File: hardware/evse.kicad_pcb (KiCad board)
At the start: 2 copper layers, 42.5 x 62.5 mm, 85 parts, among them J101 Boot, P101 CON-SENSOR2, P102 Relay, P104 12V/Motor/GP, P105 CP/PP/PE, U101 XMC1100, U102 PEM1-S12-D12-S, U103 MAX14850, U104 ADS1118I, U105 OPA171AIDBV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

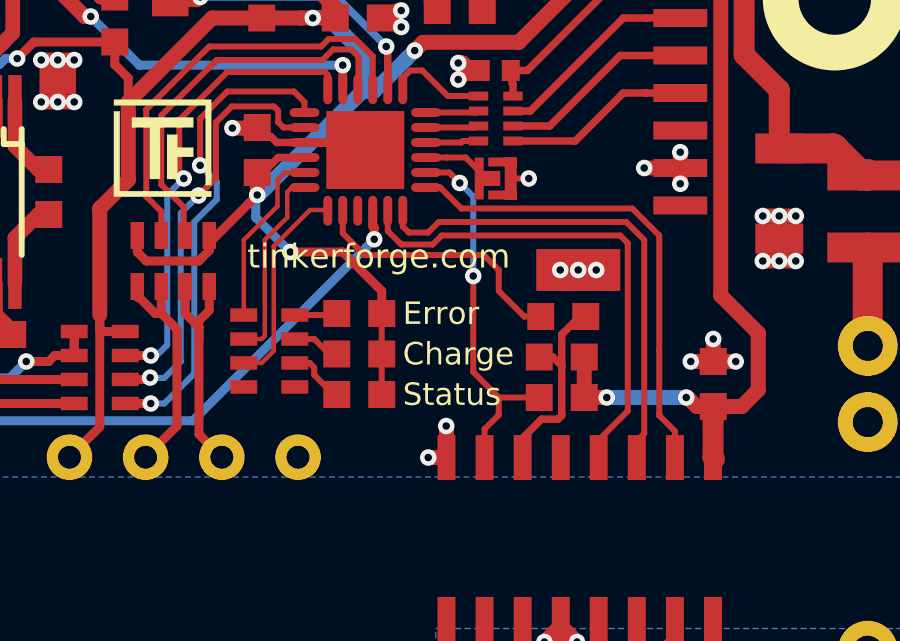
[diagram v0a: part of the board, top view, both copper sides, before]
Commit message: fix m-cs and pwm signal shift
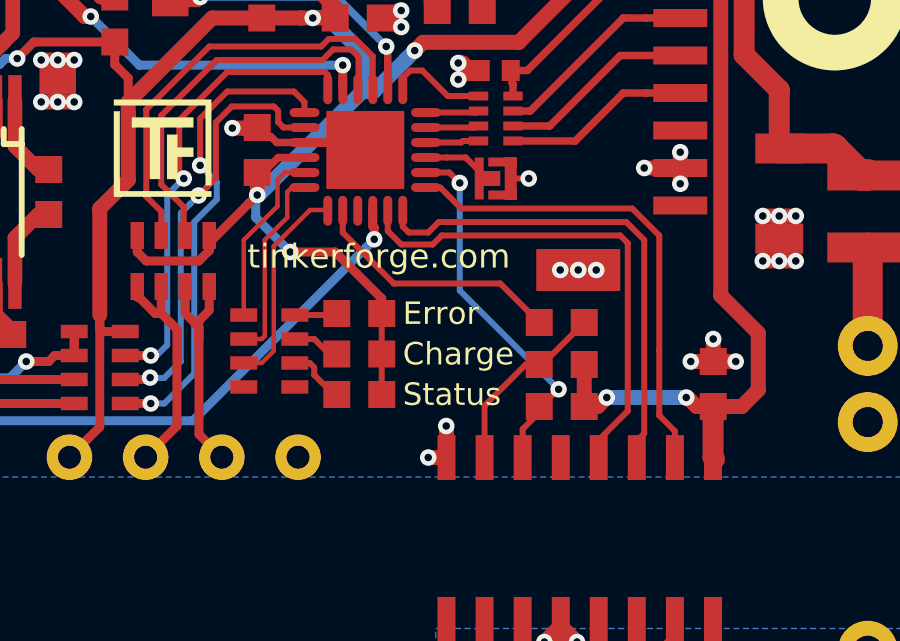
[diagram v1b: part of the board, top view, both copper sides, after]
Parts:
- moved R102 1.65 mm to (168.9, 85.0)
- moved R103 1.10 mm to (168.9, 83.7)
- moved R101 0.21 mm to (168.9, 82.2)
- renumbered Ce to C105
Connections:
- R102 pad 1: Net-(R101-Pad1) -> M-CS
- R103 pad 1: M-CS -> Net-(R101-Pad1)
- U103 pad 6: Net-(R101-Pad1) -> M-CS
- U103 pad 7: M-CS -> Net-(R101-Pad1)
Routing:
- net Net-(R101-Pad1): track 6.83 -> 6.16 mm

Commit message: thermal improvement
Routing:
- net GND: track 85.9 -> 92.1 mm, vias 96 -> 107
- net AGND: track 79.8 -> 81.4 mm, vias 36 -> 39
- added copper zone on F.Cu, net AGND
- added copper zone on F.Cu, net GND
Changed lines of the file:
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@@
     (thickness 1.6)
     (drawings 11)
-    (tracks 1064)
+    (tracks 1094)
     (zones 0)
     (modules 85)
@@
   (layers
     (0 F.Cu signal)
-    (31 B.Cu signal)
+    (31 B.Cu signal hide)
     (32 B.Adhes user)
     (33 F.Adhes user)
@@
   (segment (start 144.1 68.95) (end 144.65 69.5) (width 0.5) (layer F.Cu) (net 2))
   (via (at 144.65 69.5) (size 0.55) (drill 0.25) (layers F.Cu B.Cu) (net 2))
+  (via (at 161.45 69.8) (size 0.55) (drill 0.25) (layers F.Cu B.Cu) (net 2))
+  (segment (start 162 69.8) (end 161.45 69.8) (width 0.5) (layer F.Cu) (net 2))
+  (via (at 160.9 69.8) (size 0.55) (drill 0.25) (layers F.Cu B.Cu) (net 2))
+  (segment (start 161.45 69.8) (end 160.9 69.8) (width 0.5) (layer F.Cu) (net 2))
+  (via (at 160.35 69.8) (size 0.55) (drill 0.25) (layers F.Cu B.Cu) (net 2))
+  (segment (start 160.9 69.8) (end 160.35 69.8) (width 0.5) (layer F.Cu) (net 2))
+  (via (at 162 68.15) (size 0.55) (drill 0.25) (layers F.Cu B.Cu) (net 2))
+  (segment (start 162 68.7) (end 162 68.15) (width 0.5) (layer F.Cu) (net 2))
+  (via (at 161.45 68.15) (size 0.55) (drill 0.25) (layers F.Cu B.Cu) (net 2))
+  (segment (start 162 68.15) (end 161.45 68.15) (width 0.5) (layer F.Cu) (net 2))
+  (via (at 162.55 68.15) (size 0.55) (drill 0.25) (layers F.Cu B.Cu) (net 2))
+  (segment (start 162 68.15) (end 162.55 68.15) (width 0.5) (layer F.Cu) (net 2))
+  (via (at 160.082553 69.309927) (size 0.55) (drill 0.25) (layers F.Cu B.Cu) (net 2))
+  (segment (start 160.35 69.8) (end 160.35 69.577374) (width 0.5) (layer F.Cu) (net 2))
+  (segment (start 160.35 69.577374) (end 160.082553 69.309927) (width 0.5) (layer F.Cu) (net 2))
+  (via (at 160.082553 70.290073) (size 0.55) (drill 0.25) (layers F.Cu B.Cu) (net 2))
+  (segment (start 160.35 69.8) (end 160.35 70.022626) (width 0.5) (layer F.Cu) (net 2))
+  (segment (start 160.35 70.022626) (end 160.082553 70.290073) (width 0.5) (layer F.Cu) (net 2))
+  (via (at 160.9 68.15) (size 0.55) (drill 0.25) (layers F.Cu B.Cu) (net 2))
+  (segment (start 161.45 68.15) (end 160.9 68.15) (width 0.5) (layer F.Cu) (net 2))
+  (via (at 163.1 68.15) (size 0.55) (drill 0.25) (layers F.Cu B.Cu) (net 2))
+  (segment (start 162.55 68.15) (end 163.1 68.15) (width 0.5) (layer F.Cu) (net 2))
+  (via (at 160.35 68.15) (size 0.55) (drill 0.25) (layers F.Cu B.Cu) (net 2))
+  (segment (start 160.9 68.15) (end 160.35 68.15) (width 0.5) (layer F.Cu) (net 2))
   (segment (start 176.45 106.8) (end 175.9 107.35) (width 0.3) (layer F.Cu) (net 3))
   (segment (start 177.2 106.8) (end 176.45 106.8) (width 0.3) (layer F.Cu) (net 3))
@@
   (segment (start 149.55 113.85) (end 153.1 113.85) (width 1) (layer B.Cu) (net 6))
   (segment (start 149.54982 113.85) (end 151.2 113.85) (width 0.3) (layer B.Cu) (net 6))
+  (via (at 174.65 97.75) (size 0.55) (drill 0.25) (layers F.Cu B.Cu) (net 6))
+  (segment (start 174.1 97.75) (end 174.65 97.75) (width 0.5) (layer F.Cu) (net 6))
+  (via (at 174.65 97.2) (size 0.55) (drill 0.25) (layers F.Cu B.Cu) (net 6))
+  (segment (start 174.65 97.75) (end 174.65 97.2) (width 0.5) (layer F.Cu) (net 6))
+  (via (at 174.65 98.3) (size 0.55) (drill 0.25) (layers F.Cu B.Cu) (net 6))
+  (segment (start 174.65 97.75) (end 174.65 98.3) (width 0.5) (layer F.Cu) (net 6))
   (segment (start 174.95 104.70107) (end 174.5 104.25107) (width 0.3) (layer F.Cu) (net 7))
   (segment (start 174.95 105.40112) (end 174.95 104.70107) (width 0.3) (layer F.Cu) (net 7))
@@
       )
     )
+  )
+  (zone (net 2) (net_name GND) (layer F.Cu) (hatch edge 0.508)
+    (connect_pads yes (clearance 0))
+    (min_thickness 0.254)
+    (fill yes (arc_segments 32) (thermal_gap 0.508) (thermal_bridge_width 0.508))
+    (polygon
+      (pts
+        (xy 163.65 71.35) (xy 159.8 71.35) (xy 159.8 67.85) (xy 163.65 67.85)
+      )
+    )
+  )
+  (zone (net 6) (net_name AGND) (layer F.Cu) (hatch edge 0.508)
+    (connect_pads yes (clearance 0))
+    (min_thickness 0.254)
+    (fill yes (arc_segments 32) (thermal_gap 0.508) (thermal_bridge_width 0.508))
+    (polygon
+      (pts
+        (xy 175.2 98.9) (xy 171.4 98.9) (xy 171.4 96.5) (xy 175.2 96.5)
+      )
+    )

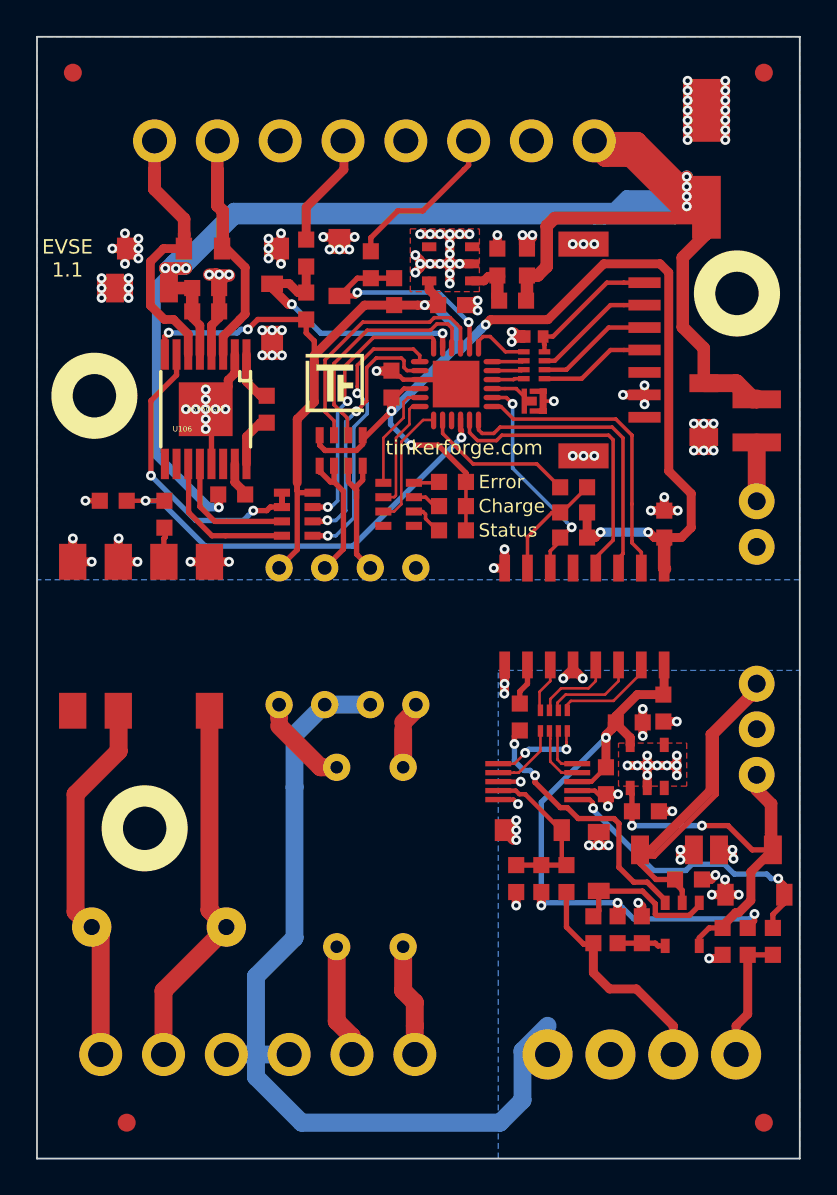
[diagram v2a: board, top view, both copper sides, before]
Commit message: change p105 pinout, add description text
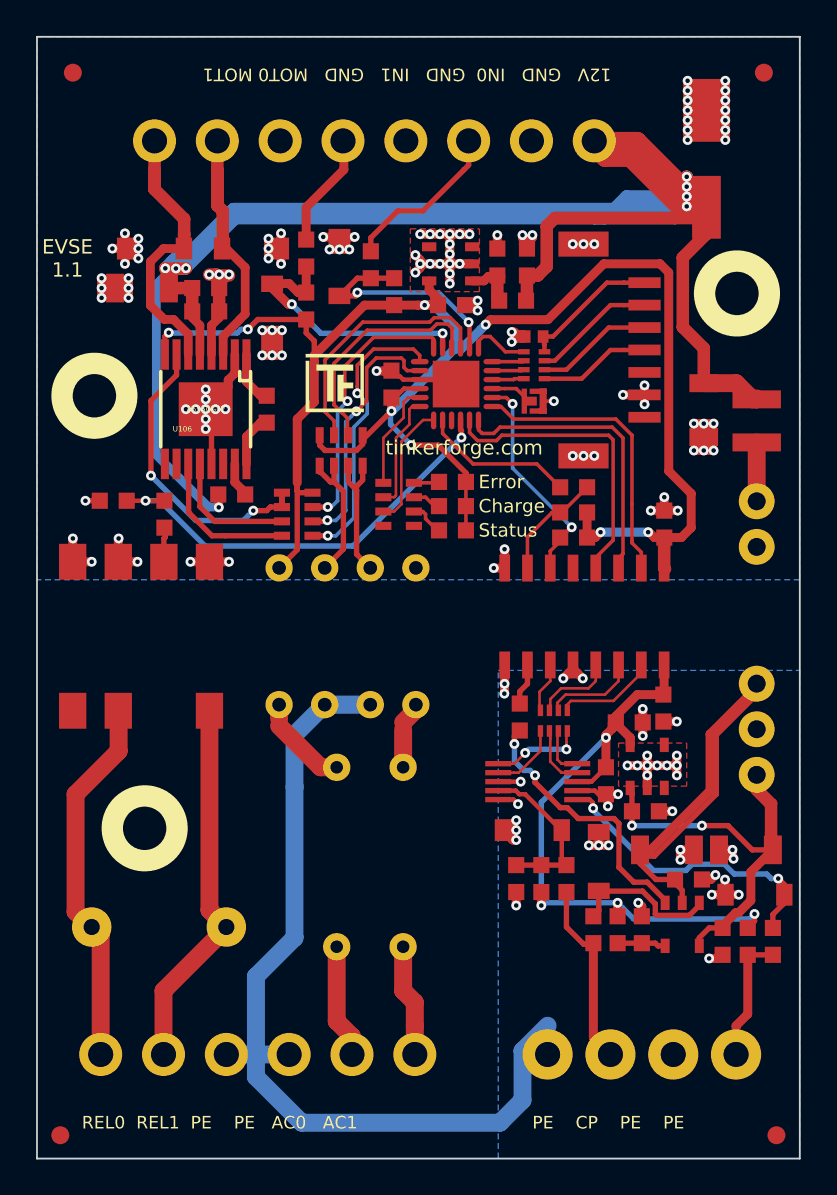
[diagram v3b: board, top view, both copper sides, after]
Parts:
- C105: value 100uF/35V -> 68uF/25V
- R102, R103: value 1k -> 10k
- moved Fiducial_Mark 3.77 mm to (140.3, 118.3)
- moved Fiducial_Mark 0.99 mm to (180.2, 118.3)
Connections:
- P105 pad 2: AGND -> Net-(P105-Pad2)
- P105 pad 3: Net-(P105-Pad3) -> AGND
- R107 pad 2: Net-(P105-Pad3) -> Net-(P105-Pad2)
- R108 pad 2: Net-(P105-Pad3) -> Net-(P105-Pad2)
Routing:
- net Net-(P105-Pad3): track 12.8 -> 0.00 mm
- net Net-(P105-Pad2): track 0.00 -> 10.4 mm
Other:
- board text added: "12V GND IN0 GND IN1 GND MOT0 MOT1"
- board text added: "PE CP PE PE"
- board text added: "REL0 REL1 PE PE AC0 AC1"
- board text removed: "Change Pin 2 + 3 for better PP resistor connection"
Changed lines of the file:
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@@
   (general
     (thickness 1.6)
-    (drawings 11)
-    (tracks 1094)
+    (drawings 13)
+    (tracks 1091)
     (zones 0)
     (modules 85)
@@
   (net 84 "Net-(P104-Pad3)")
   (net 85 "Net-(P104-Pad5)")
-  (net 86 "Net-(P105-Pad3)")
-  (net 87 "Net-(P105-Pad4)")
+  (net 86 "Net-(P105-Pad4)")
+  (net 87 "Net-(P105-Pad2)")
   (net_class Default "This is the default net class."
     (clearance 0.149)
@@
     (add_net "Net-(P104-Pad3)")
     (add_net "Net-(P104-Pad5)")
-    (add_net "Net-(P105-Pad3)")
+    (add_net "Net-(P105-Pad2)")
     (add_net "Net-(P105-Pad4)")
     (add_net "Net-(R101-Pad1)")
@@
   )
   (module kicad-libraries:Fiducial_Mark (layer F.Cu)
-    (at 144 117.65)
+    (at 140.3 118.35)
     (attr smd)
     (fp_text reference Fiducial_Mark (at 0 0) (layer F.SilkS) hide
@@
   )
   (module kicad-libraries:Fiducial_Mark (layer F.Cu)
-    (at 179.5 117.65)
+    (at 180.2 118.35)
     (attr smd)
     (fp_text reference Fiducial_Mark (at 0 0) (layer F.SilkS) hide
@@
       (effects (font (size 0.59944 0.59944) (thickness 0.12446)))
     )
-    (fp_text value 100uF/35V (at 0.95 -0.375 90) (layer F.Fab)
+    (fp_text value 68uF/25V (at 0.95 -0.375 90) (layer F.Fab)
       (effects (font (size 0.59944 0.59944) (thickness 0.12446)))
     )
@@
       (effects (font (size 0.2 0.2) (thickness 0.05)))
     )
-    (fp_text value 1k (at 0.05 -0.375) (layer F.Fab)
+    (fp_text value 10k (at 0.05 -0.375) (layer F.Fab)
       (effects (font (size 0.2 0.2) (thickness 0.05)))
     )
@@
       (effects (font (size 0.2 0.2) (thickness 0.05)))
     )
-    (fp_text value 1k (at 0.05 -0.375) (layer F.Fab)
+    (fp_text value 10k (at 0.05 -0.375) (layer F.Fab)
       (effects (font (size 0.2 0.2) (thickness 0.05)))
     )
@@
       (net 61 "Net-(D105-Pad1)"))
     (pad 2 smd rect (at 0.75 0 270) (size 0.9 0.9) (layers F.Cu F.Paste F.Mask)
-      (net 86 "Net-(P105-Pad3)"))
+      (net 87 "Net-(P105-Pad2)"))
     (model Resistors_SMD/R_0603.wrl
       (at (xyz 0 0 0))
@@
       (net 62 "Net-(D106-Pad1)"))
     (pad 2 smd rect (at 0.75 0 270) (size 0.9 0.9) (layers F.Cu F.Paste F.Mask)
-      (net 86 "Net-(P105-Pad3)"))
+      (net 87 "Net-(P105-Pad2)"))
     (model Resistors_SMD/R_0603.wrl
       (at (xyz 0 0 0))
@@
       (net 5 VEE))
     (pad 1 smd rect (at -0.75 0 90) (size 0.9 0.9) (layers F.Cu F.Paste F.Mask)
-      (net 87 "Net-(P105-Pad4)"))
+      (net 86 "Net-(P105-Pad4)"))
     (model Resistors_SMD/R_0603.wrl
       (at (xyz 0 0 0))
@@
       (net 70 "Net-(D107-Pad1)"))
     (pad 1 smd rect (at -0.75 0 90) (size 0.9 0.9) (layers F.Cu F.Paste F.Mask)
-      (net 87 "Net-(P105-Pad4)"))
+      (net 86 "Net-(P105-Pad4)"))
     (model Resistors_SMD/R_0603.wrl
       (at (xyz 0 0 0))
@@
     (fp_line (start 7.6 2.8) (end -7.6 2.8) (layer F.Fab) (width 0.12))
     (pad 2 thru_hole circle (at -1.75 0) (size 2.8 2.8) (drill 1.4) (layers *.Cu *.Mask)
-      (net 6 AGND))
+      (net 87 "Net-(P105-Pad2)"))
     (pad 3 thru_hole circle (at 1.75 0) (size 2.8 2.8) (drill 1.4) (layers *.Cu *.Mask)
-      (net 86 "Net-(P105-Pad3)"))
+      (net 6 AGND))
     (pad 1 thru_hole circle (at -5.25 0) (size 2.8 2.8) (drill 1.4) (layers *.Cu *.Mask)
       (net 6 AGND))
     (pad 4 thru_hole circle (at 5.25 0) (size 2.8 2.8) (drill 1.4) (layers *.Cu *.Mask)
-      (net 87 "Net-(P105-Pad4)"))
+      (net 86 "Net-(P105-Pad4)"))
     (model "Connectors/OQ 4P vertical.wrl"
       (at (xyz 0 0 0))
@@
     )
   )
-  (gr_text "Change Pin 2 + 3 for better PP resistor connection" (at 172.2 123.25) (layer F.Fab)
-    (effects (font (size 1 1) (thickness 0.15)))
+  (gr_text "12V   GND   IN0  GND   IN1   GND   MOT0 MOT1" (at 171 59.25 180) (layer F.SilkS)
+    (effects (font (size 0.7 0.7) (thickness 0.15)) (justify left))
+  )
+  (gr_text "REL0  REL1  PE    PE   AC0   AC1" (at 141.5 117.65) (layer F.SilkS)
+    (effects (font (size 0.7 0.7) (thickness 0.15)) (justify left))
+  )
+  (gr_text "PE    CP    PE    PE" (at 166.6 117.65) (layer F.SilkS)
+    (effects (font (size 0.7 0.7) (thickness 0.15)) (justify left))
   )
   (gr_text tinkerforge.com (at 162.8 80.05) (layer F.SilkS)
@@
   (segment (start 156.1 64.55) (end 156.1 63) (width 0.5) (layer F.Cu) (net 85))
   (segment (start 156.1 63) (end 156.05 62.95) (width 0.5) (layer F.Cu) (net 85))
-  (segment (start 168.5 104.8) (end 168.5 106.75) (width 0.3) (layer F.Cu) (net 86))
-  (segment (start 168.5 106.75) (end 169.45 107.7) (width 0.3) (layer F.Cu) (net 86))
-  (segment (start 169.45 107.7) (end 170 107.7) (width 0.3) (layer F.Cu) (net 86))
-  (segment (start 174.45 112.25) (end 172.4 110.2) (width 0.5) (layer F.Cu) (net 86))
-  (segment (start 172.4 110.2) (end 170.9 110.2) (width 0.5) (layer F.Cu) (net 86))
-  (segment (start 170.9 110.2) (end 170 109.3) (width 0.5) (layer F.Cu) (net 86))
-  (segment (start 170 109.3) (end 170 107.65) (width 0.5) (layer F.Cu) (net 86))
-  (segment (start 174.45 112.25) (end 174.45 113.85) (width 0.5) (layer F.Cu) (net 86))
-  (segment (start 180 108.3) (end 178.65 108.3) (width 0.3) (layer F.Cu) (net 87))
-  (segment (start 178.65 108.3) (end 178.6 108.35) (width 0.3) (layer F.Cu) (net 87))
-  (segment (start 178.6 108.3) (end 178.6 111.6) (width 0.5) (layer F.Cu) (net 87))
-  (segment (start 178.6 111.6) (end 177.95 112.25) (width 0.5) (layer F.Cu) (net 87))
-  (segment (start 177.95 112.25) (end 177.95 113.85) (width 0.5) (layer F.Cu) (net 87))
+  (segment (start 168.5 104.8) (end 168.5 106.75) (width 0.3) (layer F.Cu) (net 87))
+  (segment (start 168.5 106.75) (end 169.45 107.7) (width 0.3) (layer F.Cu) (net 87))
+  (segment (start 169.45 107.7) (end 170 107.7) (width 0.3) (layer F.Cu) (net 87))
+  (segment (start 180 108.3) (end 178.65 108.3) (width 0.3) (layer F.Cu) (net 86))
+  (segment (start 178.65 108.3) (end 178.6 108.35) (width 0.3) (layer F.Cu) (net 86))
+  (segment (start 178.6 108.3) (end 178.6 111.6) (width 0.5) (layer F.Cu) (net 86))
+  (segment (start 178.6 111.6) (end 177.95 112.25) (width 0.5) (layer F.Cu) (net 86))
+  (segment (start 177.95 112.25) (end 177.95 113.85) (width 0.5) (layer F.Cu) (net 86))
+  (segment (start 170 107.65) (end 170 112.9) (width 0.5) (layer F.Cu) (net 87))
+  (segment (start 170 112.9) (end 170.95 113.85) (width 0.5) (layer F.Cu) (net 87))
   (zone (net 6) (net_name AGND) (layer B.Cu) (hatch edge 0.508)
     (connect_pads yes (clearance 0))
